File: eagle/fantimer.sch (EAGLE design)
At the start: 14 parts, among them IC3 PIC10F220, K1 PB2032-ND, Q1 2N7000-G, U1 IRM-01-5, X1 732-10957-ND

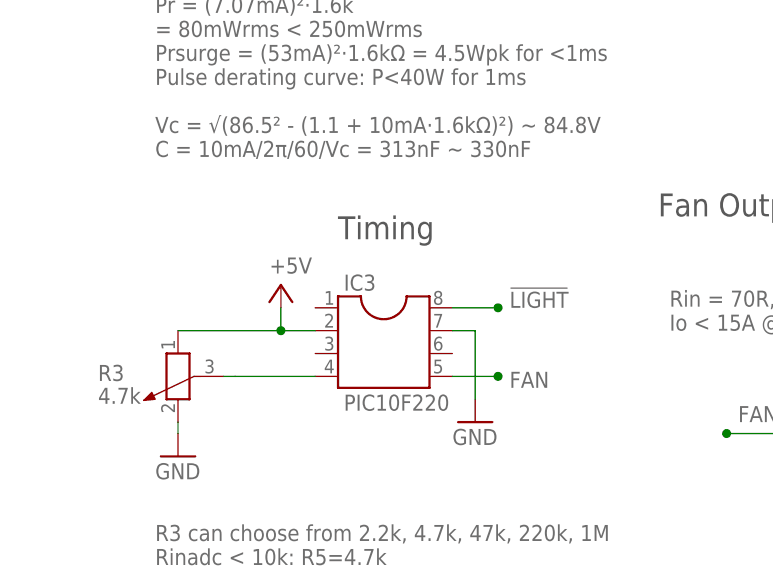
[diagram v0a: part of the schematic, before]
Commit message: Renumber IC3 to IC1
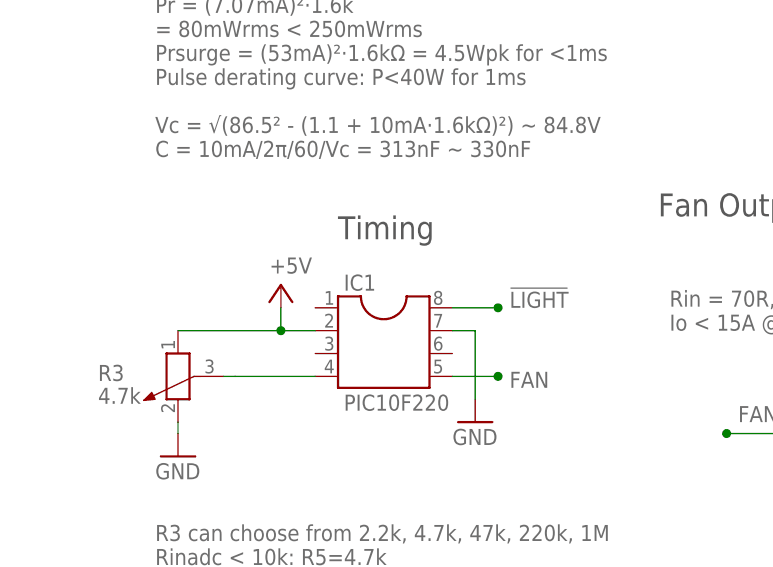
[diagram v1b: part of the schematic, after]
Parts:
- renumbered IC3 to IC1
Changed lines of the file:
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@@
 <part name="R1" library="resistor" library_urn="urn:adsk.eagle:library:348" deviceset="R-US_" device="0207/7" package3d_urn="urn:adsk.eagle:package:25942/1" value="1.6k"/>
 <part name="R3" library="rcl" library_urn="urn:adsk.eagle:library:334" deviceset="POTENTIOMETER_" device="PT-10" package3d_urn="urn:adsk.eagle:package:23786/1" value="4.7k"/>
-<part name="IC3" library="ic-package" library_urn="urn:adsk.eagle:library:239" deviceset="DIL8" device="" package3d_urn="urn:adsk.eagle:package:14440/1" value="PIC10F220"/>
+<part name="IC1" library="ic-package" library_urn="urn:adsk.eagle:library:239" deviceset="DIL8" device="" package3d_urn="urn:adsk.eagle:package:14440/1" value="PIC10F220"/>
 <part name="P+6" library="supply1" library_urn="urn:adsk.eagle:library:371" deviceset="+5V" device=""/>
 <part name="GND5" library="supply1" library_urn="urn:adsk.eagle:library:371" deviceset="GND" device=""/>
@@
 <attribute name="VALUE" x="1.27" y="43.18" size="1.778" layer="96" rot="MR180"/>
 </instance>
-<instance part="IC3" gate="G$1" x="33.02" y="49.53"/>
+<instance part="IC1" gate="G$1" x="33.02" y="49.53"/>
 <instance part="P+6" gate="1" x="21.59" y="54.61" smashed="yes">
 <attribute name="VALUE" x="20.32" y="55.88" size="1.778" layer="96"/>
@@
 <segment>
 <pinref part="GND5" gate="1" pin="GND"/>
-<pinref part="IC3" gate="G$1" pin="7"/>
+<pinref part="IC1" gate="G$1" pin="7"/>
 <wire x1="43.18" y1="41.91" x2="43.18" y2="49.53" width="0.1524" layer="91"/>
 <wire x1="43.18" y1="49.53" x2="40.64" y2="49.53" width="0.1524" layer="91"/>
@@
 <label x="46.99" y="43.18" size="1.778" layer="95"/>
 <wire x1="40.64" y1="44.45" x2="45.72" y2="44.45" width="0.1524" layer="91"/>
-<pinref part="IC3" gate="G$1" pin="5"/>
+<pinref part="IC1" gate="G$1" pin="5"/>
 </segment>
 </net>
@@
 </segment>
 <segment>
-<pinref part="IC3" gate="G$1" pin="8"/>
+<pinref part="IC1" gate="G$1" pin="8"/>
 <wire x1="40.64" y1="52.07" x2="45.72" y2="52.07" width="0.1524" layer="91"/>
 <junction x="45.72" y="52.07"/>
@@
 <pinref part="R3" gate="1" pin="3"/>
 <wire x1="15.24" y1="44.45" x2="16.51" y2="44.45" width="0.1524" layer="91"/>
-<pinref part="IC3" gate="G$1" pin="4"/>
+<pinref part="IC1" gate="G$1" pin="4"/>
 <wire x1="25.4" y1="44.45" x2="16.51" y2="44.45" width="0.1524" layer="91"/>
 </segment>
@@
 <segment>
 <pinref part="P+6" gate="1" pin="+5V"/>
-<pinref part="IC3" gate="G$1" pin="2"/>
+<pinref part="IC1" gate="G$1" pin="2"/>
 <wire x1="21.59" y1="52.07" x2="21.59" y2="49.53" width="0.1524" layer="91"/>
 <wire x1="21.59" y1="49.53" x2="25.4" y2="49.53" width="0.1524" layer="91"/>

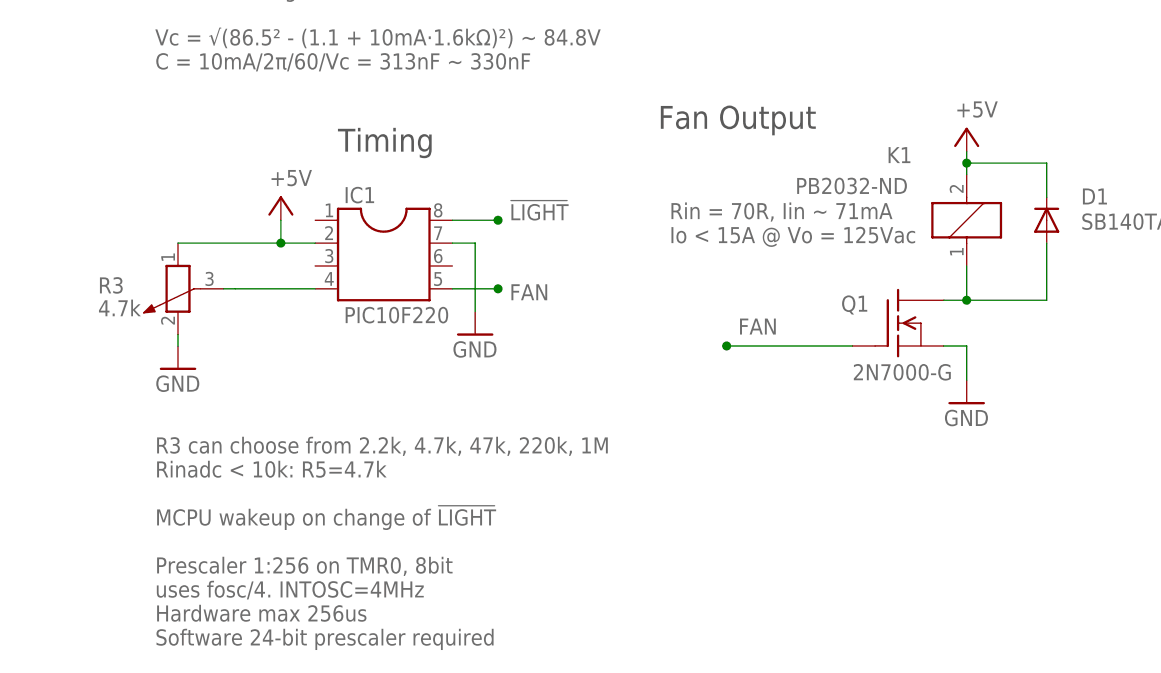
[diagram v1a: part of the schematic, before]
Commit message: Initial assembly. Add a better PIC Eagle lib. Remove PIC notes from sch.
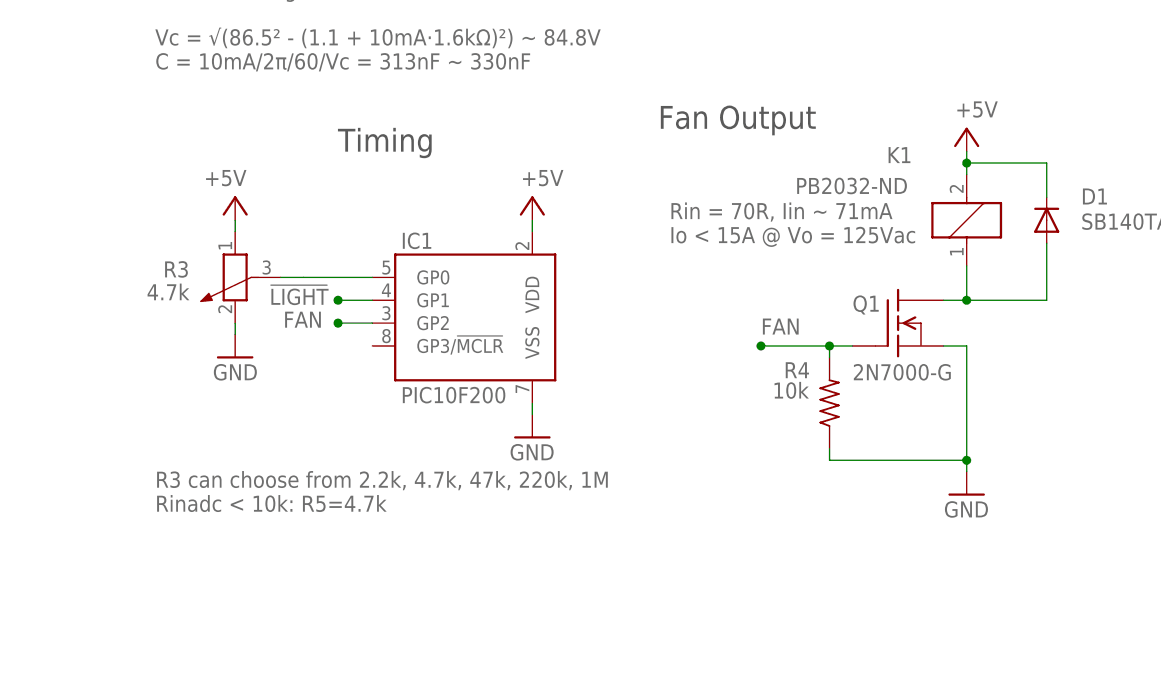
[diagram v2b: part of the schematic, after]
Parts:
- added R4: 10k, resistor:R-US_0207/7
- IC1: value PIC10F220 -> PIC10F200; device ic-package:DIL8 -> microchip-addl:PIC10F220-I/P
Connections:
- removed net RTIMER: IC1.4, R3.3
- new net ADJ: IC1.GP0, R3.3
- net !LIGHT: now also IC1.GP1; no longer IC1.8
- net +5V: now also IC1.VDD; no longer IC1.2
- net FAN: now also IC1.GP2, R4.2; no longer IC1.5
- net GND: now also IC1.VSS, R4.1; no longer IC1.7
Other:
- note added: "R3 can choose from 2.2k, 4.7k, 47k, 220k, 1M Rinadc < 10k: R5=4.7k"
- note removed: "R3 can choose from 2.2k, 4.7k, 47k, 220k, 1M Rinadc < 10k: R5=4.7k MCPU wakeup on change of !LIGHT Prescaler 1:256 on TMR0, 8bit uses fosc/4. INTOSC=4MHz Hardware max 256us Software 24-bit prescaler required"
- moved on the sheet: IC1, R3
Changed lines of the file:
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@@
 <part name="R1" library="resistor" library_urn="urn:adsk.eagle:library:348" deviceset="R-US_" device="0207/7" package3d_urn="urn:adsk.eagle:package:25942/1" value="1.6k"/>
 <part name="R3" library="rcl" library_urn="urn:adsk.eagle:library:334" deviceset="POTENTIOMETER_" device="PT-10" package3d_urn="urn:adsk.eagle:package:23786/1" value="4.7k"/>
-<part name="IC1" library="ic-package" library_urn="urn:adsk.eagle:library:239" deviceset="DIL8" device="" package3d_urn="urn:adsk.eagle:package:14440/1" value="PIC10F220"/>
 <part name="P+6" library="supply1" library_urn="urn:adsk.eagle:library:371" deviceset="+5V" device=""/>
 <part name="GND5" library="supply1" library_urn="urn:adsk.eagle:library:371" deviceset="GND" device=""/>
-<part name="GND7" library="supply1" library_urn="urn:adsk.eagle:library:371" deviceset="GND" device=""/>
 <part name="C3" library="rcl" library_urn="urn:adsk.eagle:library:334" deviceset="C-EU" device="025-025X050" package3d_urn="urn:adsk.eagle:package:23629/2" value="1uF"/>
+<part name="P+2" library="supply1" library_urn="urn:adsk.eagle:library:371" deviceset="+5V" device=""/>
+<part name="IC1" library="microchip-addl" deviceset="PIC10F220" device="-I/P" package3d_urn="urn:adsk.eagle:package:14440/1" value="PIC10F200"/>
+<part name="GND2" library="supply1" library_urn="urn:adsk.eagle:library:371" deviceset="GND" device=""/>
+<part name="R4" library="resistor" library_urn="urn:adsk.eagle:library:348" deviceset="R-US_" device="0207/7" package3d_urn="urn:adsk.eagle:package:25942/1" value="10k"/>
 </parts>
 <sheets>
@@
 <plain>
 <text x="8.89" y="172.72" size="1.778" layer="96">5mm 16A 300V</text>
-<text x="7.62" y="27.94" size="1.778" layer="96" rot="MR180">R3 can choose from 2.2k, 4.7k, 47k, 220k, 1M
-Rinadc &lt; 10k: R5=4.7k
-MCPU wakeup on change of !LIGHT
-Prescaler 1:256 on TMR0, 8bit
-uses fosc/4. INTOSC=4MHz
-Hardware max 256us
-Software 24-bit prescaler required
-</text>
+<text x="7.62" y="24.13" size="1.778" layer="96" rot="MR180">R3 can choose from 2.2k, 4.7k, 47k, 220k, 1M
+Rinadc &lt; 10k: R5=4.7k</text>
 <text x="86.36" y="161.29" size="1.778" layer="96">85-305 Vac 47-63 Hz in
 5V 200mA out
@@
 </instance>
 <instance part="GND1" gate="1" x="120.65" y="171.45"/>
-<instance part="GND3" gate="1" x="97.79" y="31.75"/>
+<instance part="GND3" gate="1" x="97.79" y="21.59"/>
 <instance part="Q1" gate="G$1" x="90.17" y="40.64" smashed="yes">
 <attribute name="VALUE" x="85.09" y="34.29" size="1.778" layer="96"/>
-<attribute name="NAME" x="83.82" y="41.91" size="1.778" layer="95"/>
+<attribute name="NAME" x="85.09" y="41.91" size="1.778" layer="95"/>
 </instance>
 <instance part="K1" gate="1" x="97.79" y="52.07" smashed="yes" rot="R180">
@@
 <attribute name="VALUE" x="17.78" y="137.668" size="1.778" layer="96"/>
 </instance>
-<instance part="R3" gate="1" x="10.16" y="44.45" smashed="yes" rot="MR270">
-<attribute name="NAME" x="1.27" y="45.72" size="1.778" layer="95" rot="MR180"/>
-<attribute name="VALUE" x="1.27" y="43.18" size="1.778" layer="96" rot="MR180"/>
-</instance>
-<instance part="IC1" gate="G$1" x="33.02" y="49.53"/>
-<instance part="P+6" gate="1" x="21.59" y="54.61" smashed="yes">
-<attribute name="VALUE" x="20.32" y="55.88" size="1.778" layer="96"/>
-</instance>
-<instance part="GND5" gate="1" x="43.18" y="39.37"/>
-<instance part="GND7" gate="1" x="10.16" y="35.56"/>
+<instance part="R3" gate="1" x="16.51" y="45.72" smashed="yes" rot="MR270">
+<attribute name="NAME" x="11.43" y="45.72" size="1.778" layer="95" rot="MR0"/>
+<attribute name="VALUE" x="11.43" y="43.18" size="1.778" layer="96" rot="MR0"/>
+</instance>
+<instance part="P+6" gate="1" x="49.53" y="54.61" smashed="yes">
+<attribute name="VALUE" x="48.26" y="55.88" size="1.778" layer="96"/>
+</instance>
+<instance part="GND5" gate="1" x="16.51" y="36.83" rot="MR0"/>
 <instance part="C3" gate="G$1" x="80.01" y="139.7"/>
+<instance part="P+2" gate="1" x="16.51" y="54.61" smashed="yes" rot="MR0">
+<attribute name="VALUE" x="17.78" y="55.88" size="1.778" layer="96" rot="MR0"/>
+</instance>
+<instance part="IC1" gate="G$1" x="46.99" y="44.45"/>
+<instance part="GND2" gate="1" x="49.53" y="27.94"/>
+<instance part="R4" gate="G$1" x="82.55" y="31.75" smashed="yes" rot="R90">
+<attribute name="NAME" x="77.47" y="34.5186" size="1.778" layer="95"/>
+<attribute name="VALUE" x="76.2" y="32.258" size="1.778" layer="96"/>
+</instance>
 </instances>
 <busses>
@@
 <pinref part="GND3" gate="1" pin="GND"/>
 <wire x1="95.25" y1="38.1" x2="97.79" y2="38.1" width="0.1524" layer="91"/>
-<wire x1="97.79" y1="38.1" x2="97.79" y2="34.29" width="0.1524" layer="91"/>
+<wire x1="97.79" y1="38.1" x2="97.79" y2="25.4" width="0.1524" layer="91"/>
+<pinref part="R4" gate="G$1" pin="1"/>
+<wire x1="97.79" y1="25.4" x2="97.79" y2="24.13" width="0.1524" layer="91"/>
+<wire x1="82.55" y1="26.67" x2="82.55" y2="25.4" width="0.1524" layer="91"/>
+<wire x1="82.55" y1="25.4" x2="97.79" y2="25.4" width="0.1524" layer="91"/>
+<junction x="97.79" y="25.4"/>
 </segment>
 <segment>
@@
 <segment>
 <pinref part="GND5" gate="1" pin="GND"/>
-<pinref part="IC1" gate="G$1" pin="7"/>
-<wire x1="43.18" y1="41.91" x2="43.18" y2="49.53" width="0.1524" layer="91"/>
-<wire x1="43.18" y1="49.53" x2="40.64" y2="49.53" width="0.1524" layer="91"/>
-</segment>
-<segment>
+<wire x1="16.51" y1="39.37" x2="16.51" y2="40.64" width="0.1524" layer="91"/>
 <pinref part="R3" gate="1" pin="2"/>
-<pinref part="GND7" gate="1" pin="GND"/>
-<wire x1="10.16" y1="39.37" x2="10.16" y2="38.1" width="0.1524" layer="91"/>
+</segment>
+<segment>
+<pinref part="IC1" gate="G$1" pin="VSS"/>
+<pinref part="GND2" gate="1" pin="GND"/>
+<wire x1="49.53" y1="31.75" x2="49.53" y2="30.48" width="0.1524" layer="91"/>
 </segment>
 </net>
 <net name="FAN" class="0">
 <segment>
-<wire x1="71.12" y1="38.1" x2="85.09" y2="38.1" width="0.1524" layer="91"/>
+<wire x1="74.93" y1="38.1" x2="82.55" y2="38.1" width="0.1524" layer="91"/>
 <pinref part="Q1" gate="G$1" pin="G"/>
-<label x="72.39" y="39.37" size="1.778" layer="95"/>
-<junction x="71.12" y="38.1"/>
-</segment>
-<segment>
-<junction x="45.72" y="44.45"/>
-<label x="46.99" y="43.18" size="1.778" layer="95"/>
-<wire x1="40.64" y1="44.45" x2="45.72" y2="44.45" width="0.1524" layer="91"/>
-<pinref part="IC1" gate="G$1" pin="5"/>
+<label x="74.93" y="39.37" size="1.778" layer="95"/>
+<junction x="74.93" y="38.1"/>
+<pinref part="R4" gate="G$1" pin="2"/>
+<wire x1="82.55" y1="38.1" x2="85.09" y2="38.1" width="0.1524" layer="91"/>
+<wire x1="82.55" y1="36.83" x2="82.55" y2="38.1" width="0.1524" layer="91"/>
+<junction x="82.55" y="38.1"/>
+</segment>
+<segment>
+<wire x1="31.75" y1="40.64" x2="27.94" y2="40.64" width="0.1524" layer="91"/>
+<junction x="27.94" y="40.64"/>
+<label x="21.844" y="40.132" size="1.778" layer="95"/>
+<pinref part="IC1" gate="G$1" pin="GP2"/>
 </segment>
 </net>
@@
 </segment>
 <segment>
-<pinref part="IC1" gate="G$1" pin="8"/>
-<wire x1="40.64" y1="52.07" x2="45.72" y2="52.07" width="0.1524" layer="91"/>
-<junction x="45.72" y="52.07"/>
-<label x="46.99" y="52.07" size="1.778" layer="95"/>
+<wire x1="31.75" y1="43.18" x2="27.94" y2="43.18" width="0.1524" layer="91"/>
+<junction x="27.94" y="43.18"/>
+<label x="20.32" y="42.672" size="1.778" layer="95"/>
+<pinref part="IC1" gate="G$1" pin="GP1"/>
 </segment>
 </net>
@@
 <pinref part="C1" gate="G$1" pin="2"/>
 <wire x1="17.78" y1="132.08" x2="19.05" y2="132.08" width="0.1524" layer="91"/>
-</segment>
-</net>
-<net name="RTIMER" class="0">
-<segment>
-<pinref part="R3" gate="1" pin="3"/>
-<wire x1="15.24" y1="44.45" x2="16.51" y2="44.45" width="0.1524" layer="91"/>
-<pinref part="IC1" gate="G$1" pin="4"/>
-<wire x1="25.4" y1="44.45" x2="16.51" y2="44.45" width="0.1524" layer="91"/>
 </segment>
 </net>
@@
 </segment>
 <segment>
+<pinref part="R3" gate="1" pin="1"/>
+<pinref part="P+2" gate="1" pin="+5V"/>
+<wire x1="16.51" y1="50.8" x2="16.51" y2="52.07" width="0.1524" layer="91"/>
+</segment>
+<segment>
 <pinref part="P+6" gate="1" pin="+5V"/>
-<pinref part="IC1" gate="G$1" pin="2"/>
-<wire x1="21.59" y1="52.07" x2="21.59" y2="49.53" width="0.1524" layer="91"/>
-<wire x1="21.59" y1="49.53" x2="25.4" y2="49.53" width="0.1524" layer="91"/>
-<pinref part="R3" gate="1" pin="1"/>
-<wire x1="10.16" y1="49.53" x2="21.59" y2="49.53" width="0.1524" layer="91"/>
-<junction x="21.59" y="49.53"/>
-</segment>
-</net>
+<pinref part="IC1" gate="G$1" pin="VDD"/>
+<wire x1="49.53" y1="52.07" x2="49.53" y2="50.8" width="0.1524" layer="91"/>
+</segment>
+</net>
+<net name="ADJ" class="0">
+<segment>
+<pinref part="R3" gate="1" pin="3"/>
+<wire x1="21.59" y1="45.72" x2="24.13" y2="45.72" width="0.1524" layer="91"/>
+<pinref part="IC1" gate="G$1" pin="GP0"/>
+<wire x1="24.13" y1="45.72" x2="31.75" y2="45.72" width="0.1524" layer="91"/>
+</segment>
+</net>

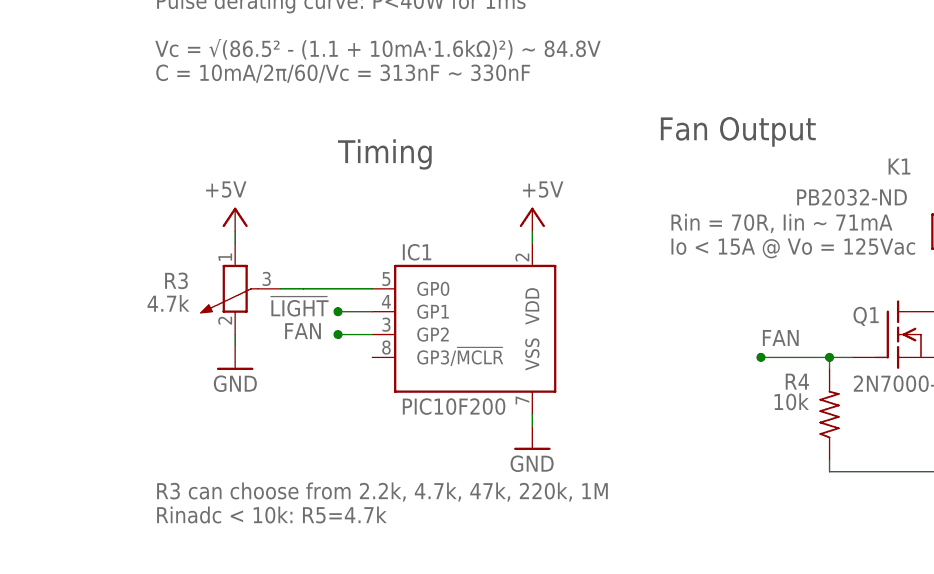
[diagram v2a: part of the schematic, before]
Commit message: Add filter cap for MCU
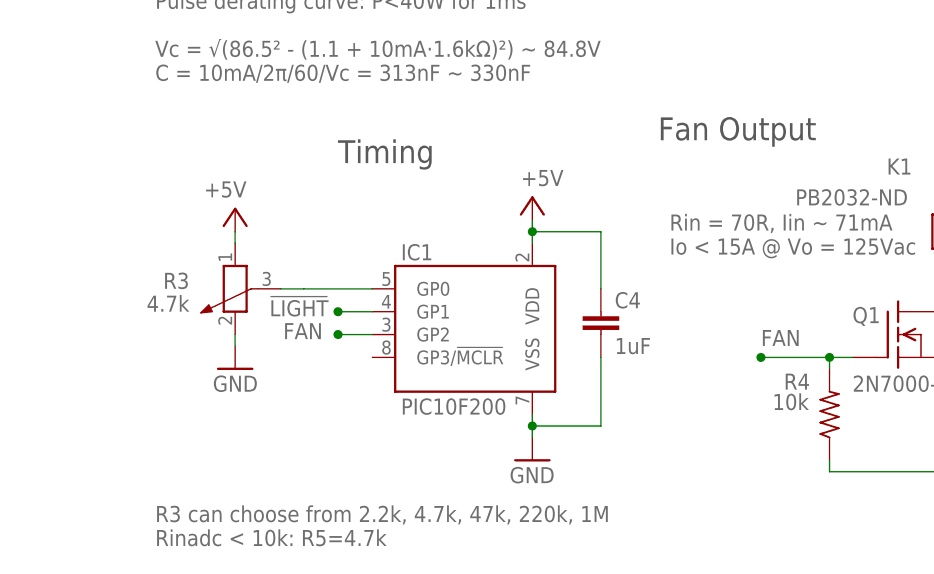
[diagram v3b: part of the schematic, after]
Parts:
- added C4: 1uF, rcl:C-EU025-025X050
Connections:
- net +5V: now also C4.1
- net GND: now also C4.2
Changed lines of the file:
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@@
 <part name="GND2" library="supply1" library_urn="urn:adsk.eagle:library:371" deviceset="GND" device=""/>
 <part name="R4" library="resistor" library_urn="urn:adsk.eagle:library:348" deviceset="R-US_" device="0207/7" package3d_urn="urn:adsk.eagle:package:25942/1" value="10k"/>
+<part name="C4" library="rcl" library_urn="urn:adsk.eagle:library:334" deviceset="C-EU" device="025-025X050" package3d_urn="urn:adsk.eagle:package:23629/2" value="1uF"/>
 </parts>
 <sheets>
@@
 <plain>
 <text x="8.89" y="172.72" size="1.778" layer="96">5mm 16A 300V</text>
-<text x="7.62" y="24.13" size="1.778" layer="96" rot="MR180">R3 can choose from 2.2k, 4.7k, 47k, 220k, 1M
+<text x="7.62" y="21.59" size="1.778" layer="96" rot="MR180">R3 can choose from 2.2k, 4.7k, 47k, 220k, 1M
 Rinadc &lt; 10k: R5=4.7k</text>
 <text x="86.36" y="161.29" size="1.778" layer="96">85-305 Vac 47-63 Hz in
@@
 <attribute name="VALUE" x="11.43" y="43.18" size="1.778" layer="96" rot="MR0"/>
 </instance>
-<instance part="P+6" gate="1" x="49.53" y="54.61" smashed="yes">
-<attribute name="VALUE" x="48.26" y="55.88" size="1.778" layer="96"/>
+<instance part="P+6" gate="1" x="49.53" y="55.88" smashed="yes">
+<attribute name="VALUE" x="48.26" y="57.15" size="1.778" layer="96"/>
 </instance>
 <instance part="GND5" gate="1" x="16.51" y="36.83" rot="MR0"/>
@@
 </instance>
 <instance part="IC1" gate="G$1" x="46.99" y="44.45"/>
-<instance part="GND2" gate="1" x="49.53" y="27.94"/>
+<instance part="GND2" gate="1" x="49.53" y="26.67"/>
 <instance part="R4" gate="G$1" x="82.55" y="31.75" smashed="yes" rot="R90">
 <attribute name="NAME" x="77.47" y="34.5186" size="1.778" layer="95"/>
 <attribute name="VALUE" x="76.2" y="32.258" size="1.778" layer="96"/>
 </instance>
+<instance part="C4" gate="G$1" x="57.15" y="43.18"/>
 </instances>
 <busses>
@@
 <pinref part="GND2" gate="1" pin="GND"/>
 <wire x1="49.53" y1="31.75" x2="49.53" y2="30.48" width="0.1524" layer="91"/>
+<pinref part="C4" gate="G$1" pin="2"/>
+<wire x1="49.53" y1="30.48" x2="49.53" y2="29.21" width="0.1524" layer="91"/>
+<wire x1="57.15" y1="38.1" x2="57.15" y2="30.48" width="0.1524" layer="91"/>
+<wire x1="57.15" y1="30.48" x2="49.53" y2="30.48" width="0.1524" layer="91"/>
+<junction x="49.53" y="30.48"/>
 </segment>
 </net>
@@
 <pinref part="P+6" gate="1" pin="+5V"/>
 <pinref part="IC1" gate="G$1" pin="VDD"/>
+<wire x1="49.53" y1="53.34" x2="49.53" y2="52.07" width="0.1524" layer="91"/>
+<pinref part="C4" gate="G$1" pin="1"/>
 <wire x1="49.53" y1="52.07" x2="49.53" y2="50.8" width="0.1524" layer="91"/>
-</segment>
-</net>
+<wire x1="57.15" y1="45.72" x2="57.15" y2="52.07" width="0.1524" layer="91"/>
+<wire x1="57.15" y1="52.07" x2="49.53" y2="52.07" width="0.1524" layer="91"/>
+<junction x="49.53" y="52.07"/>
+</segment>
+</net>
